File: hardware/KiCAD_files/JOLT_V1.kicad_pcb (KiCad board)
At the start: 2 copper layers, 71.8 x 48.5 mm, 73 parts, among them J1 Conn_01x04_Pin, J13 Conn_01x05_Pin, J2 Conn_01x10_Socket, J3 Conn_01x04_Pin, J4 XT60-M, J5 Conn_01x13_Socket, SW1 SW_Push, SW2 SW_SPDT, U1 STM32F405RGT6, U2 AMS1117-3.3, U3 PCA9685BS, U4 AMS1117-5.0, U5 ICM-42688-P, Y1 16MHz

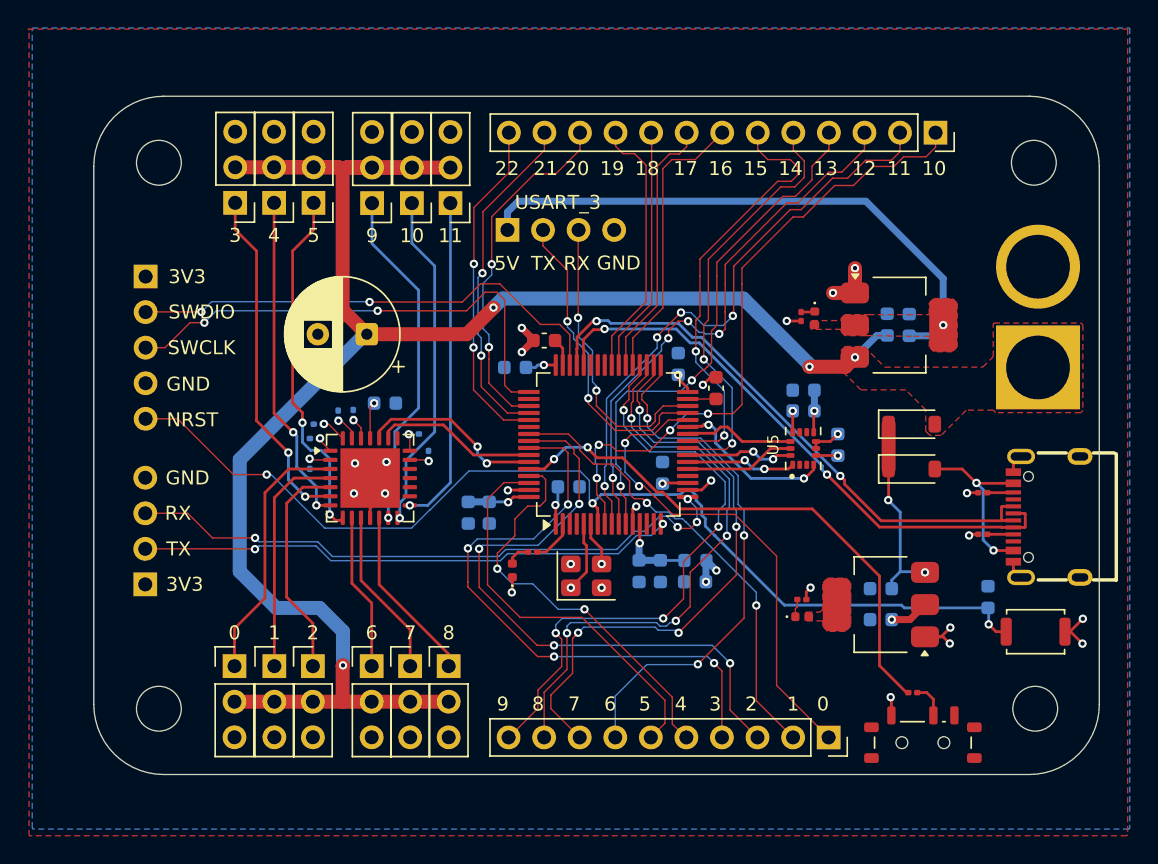
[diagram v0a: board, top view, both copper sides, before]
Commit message: Add new files after review and update readme
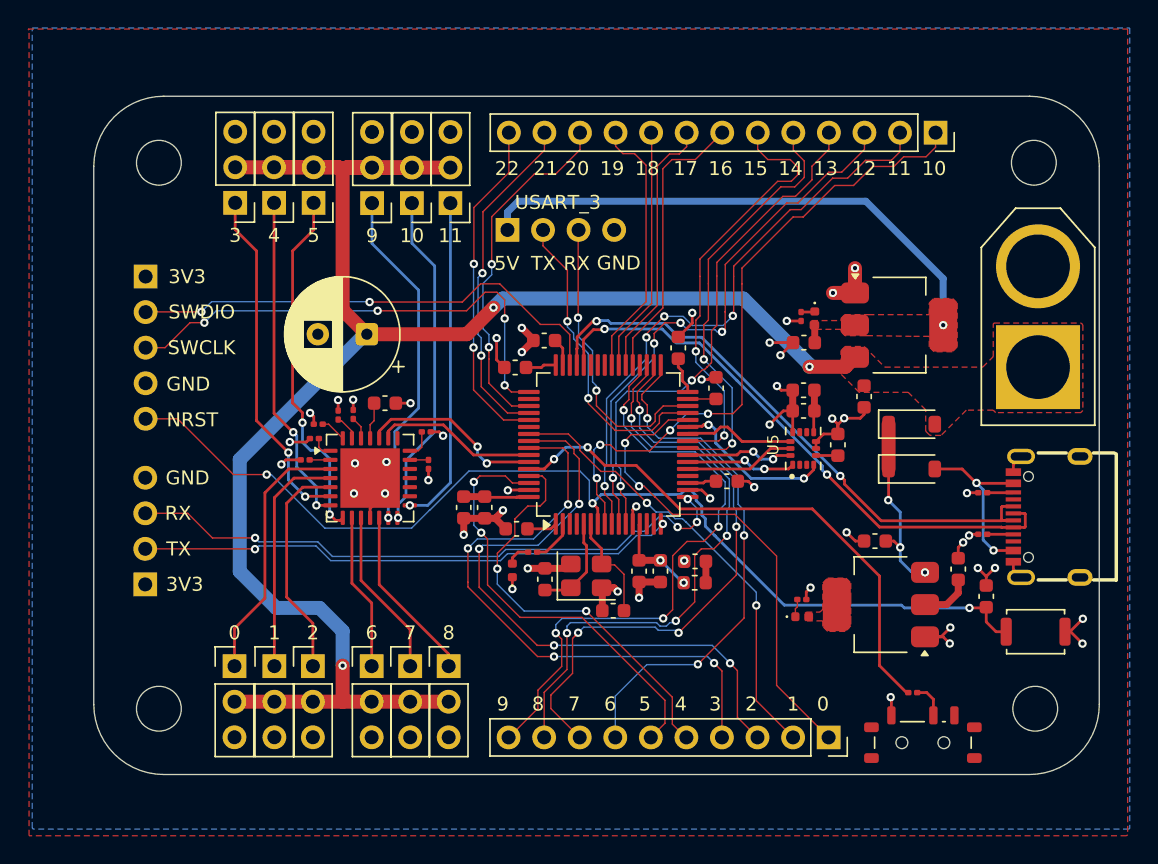
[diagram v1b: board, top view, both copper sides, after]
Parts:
- C1, C10, C11, C12, C13, C15, C16, C19, C2, C20, C21, C22, C23, C3, C4, C5, C6, C7, C8, C9, FB1, J4, R12, R13, R14, R15, R16, R17, R18: moved to F.Cu
- moved C23 7.63 mm to (168.1, 86.8), turned to 180 degrees
- moved C13 6.60 mm to (179.1, 103.0), turned to 90 degrees
- moved C22 5.40 mm to (172.4, 90.7), turned to -90 degrees
- moved C1 4.78 mm to (147.6, 100.2), turned to 180 degrees
- moved C3 4.64 mm to (162.6, 96.8), turned to 0 degrees
- moved C12 3.43 mm to (173.2, 101.0)
- moved C16 2.59 mm to (154.4, 106.0), turned to 180 degrees
- moved C15 1.72 mm to (149.6, 103.8)
- moved FB1 1.59 mm to (160.3, 104.0)
- moved C9 1.46 mm to (160.3, 102.5)
- moved C5 1.15 mm to (159.1, 87.2)
- moved R18 0.86 mm to (141.1, 93.2)
- moved R12 0.64 mm to (141.3, 95.5), turned to -90 degrees
- moved C2 0.50 mm to (145.3, 98.6)
- moved C6 0.50 mm to (143.8, 98.6)
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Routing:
- net GND: track 34.3 -> 79.3 mm, vias 26 -> 49
- net /Main/HSE_OUT: track 3.29 -> 7.69 mm, vias 1 -> 0
- net SERVO_PWR: track 131.7 -> 127.7 mm, vias 4 -> 3
- net /Main/GPIO5: track 28.7 -> 31.2 mm, vias 0 -> 2
- net /Main/HSE_IN: track 5.29 -> 7.03 mm, vias 1 -> 0
- net +5V: track 41.1 -> 39.7 mm
- net Net-(U3-A5): track 1.22 -> 2.06 mm, vias 1 -> 0
- net Net-(D4-K): track 14.2 -> 13.4 mm, vias 2 -> 3
- net /Main/GPIO9: track 43.2 -> 43.9 mm
- net /Main/GPIO4: track 29.2 -> 29.9 mm
- net +3.3VA: track 5.86 -> 6.47 mm, vias 1 -> 2
- net /Main/GPIO1: track 33.1 -> 32.6 mm
- net /Main/GPIO8: track 41.9 -> 42.4 mm
- net Net-(U3-A3): track 1.20 -> 1.55 mm, vias 1 -> 0
- net +3.3V: track 25.4 -> 25.6 mm, vias 11 -> 0
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
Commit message: Update files
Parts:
- H1, H2, H3, H4: footprint MountingHole:MountingHole_3.2mm_M3 -> MountingHole:MountingHole_3.2mm_M3_Pad_Via

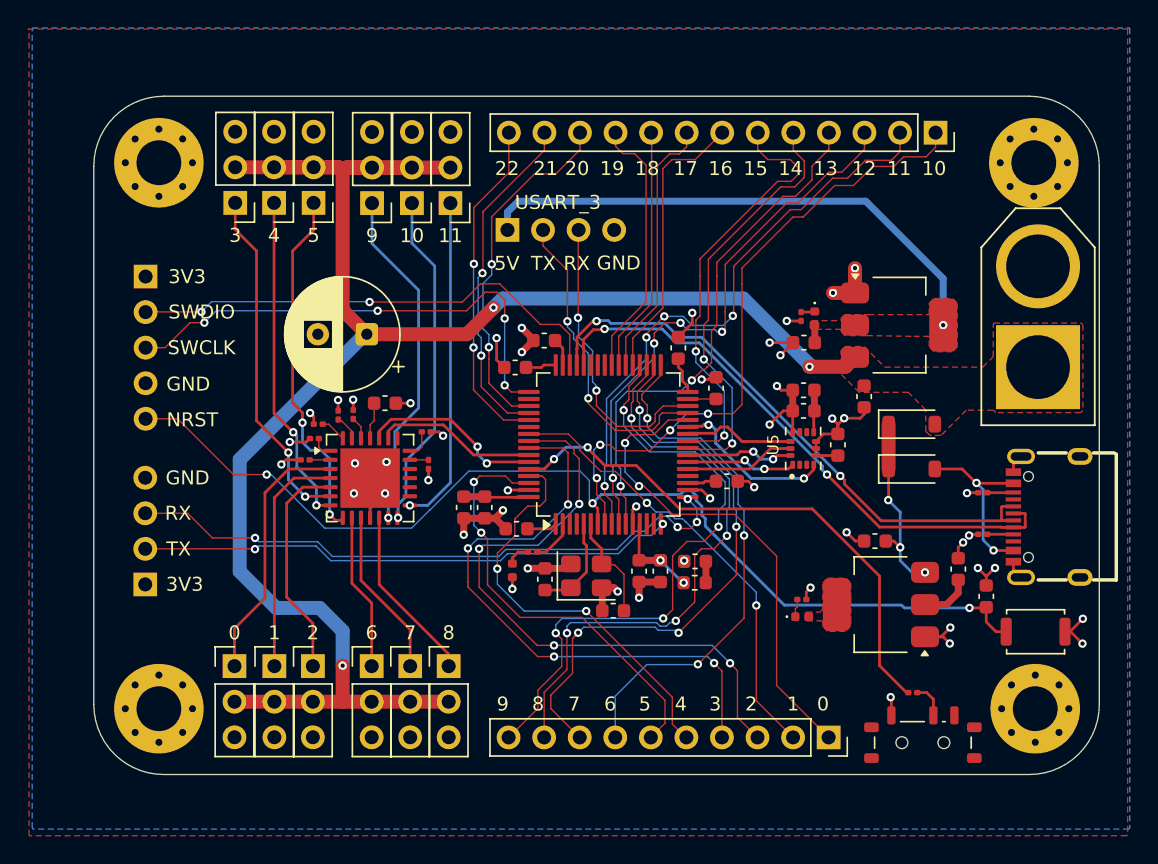
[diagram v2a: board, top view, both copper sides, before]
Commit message: Add 4 layer pcb and update readme
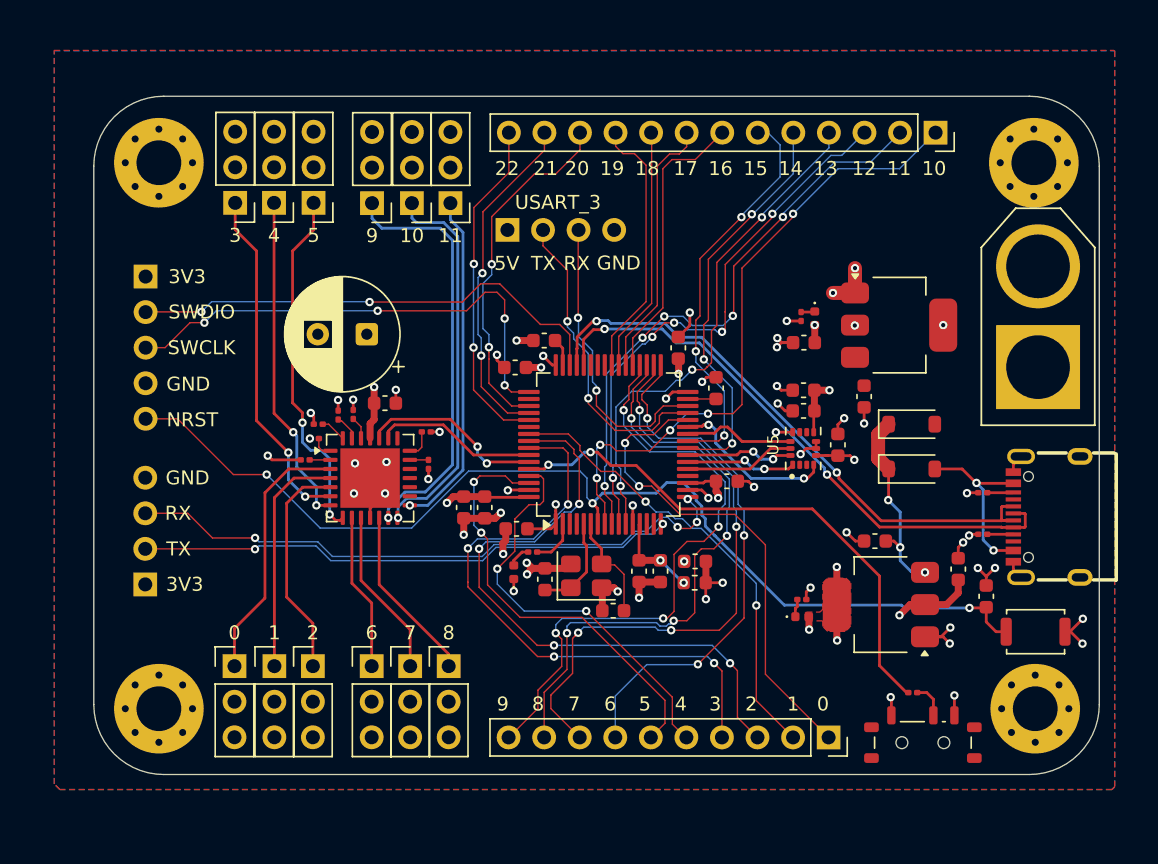
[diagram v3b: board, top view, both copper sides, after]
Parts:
- moved D1 0.16 mm to (147.3, 103.2)
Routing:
- net SERVO_PWR: track 127.7 -> 0.00 mm, vias 3 -> 0
- net +5V: track 39.7 -> 1.33 mm, vias 1 -> 3
- net +3.3V: track 25.6 -> 45.6 mm, vias 0 -> 17
- net GND: track 79.3 -> 71.5 mm, vias 49 -> 52
- net /Servo_Controller/SERVO_9: track 24.8 -> 30.1 mm
- net /Servo_Controller/SERVO_10: track 24.2 -> 27.6 mm
- net /Main/GPIO15: track 30.9 -> 28.8 mm, vias 2 -> 3
- net /Main/GPIO7: track 42.8 -> 44.2 mm
- net /Main/GPIO14: track 30.3 -> 29.2 mm, vias 2 -> 3
- net /Servo_Controller/SERVO_11: track 23.5 -> 24.3 mm
- net /Main/GPIO13: track 37.4 -> 36.7 mm, vias 2 -> 3
- net /Main/GPIO10: track 46.1 -> 45.4 mm, vias 4 -> 5
- net /Main/GPIO11: track 42.5 -> 41.8 mm, vias 4 -> 5
- net Net-(D4-K): track 13.4 -> 14.1 mm
- net /Main/GPIO12: track 40.0 -> 39.6 mm, vias 4 -> 5
- added copper zone on In1.Cu, net +3.3V
- added copper zone on B.Cu, net +5V
- added copper zone on In2.Cu, net GND
- removed copper zone on F.Cu, net +5V
- removed copper zone on B.Cu, net GND
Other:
- copper layers 2 -> 4

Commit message: Add updated kicad files
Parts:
- moved R12 0.35 mm to (141.1, 95.2)
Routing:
- net SERVO_PWR: track 0.00 -> 138.4 mm, vias 0 -> 5
- net +5V: track 1.33 -> 40.4 mm, vias 3 -> 2
- net GND: track 71.5 -> 95.7 mm
- net +3.3V: track 45.6 -> 61.5 mm, vias 17 -> 10
- net /Main/GPIO6: track 37.9 -> 38.7 mm, vias 3 -> 4
- net /Main/GPIO20: track 25.4 -> 24.7 mm
- net Net-(D4-K): track 14.1 -> 13.4 mm, vias 3 -> 4
- net /Main/USART2_TX: track 38.6 -> 38.8 mm, vias 2 -> 4
- net I2C_SCL: track 11.6 -> 11.7 mm, vias 0 -> 2
- net Net-(U1-BOOT0): vias 2 -> 4
- net /Main/USART2_RX: vias 4 -> 6
- net /Main/GPIO0: vias 2 -> 4
- added copper zone on B.Cu, net GND
- removed copper zone on In1.Cu, net +3.3V
- removed copper zone on B.Cu, net +5V
- removed copper zone on In2.Cu, net GND
- removed copper zone on F.Cu, net SERVO_PWR
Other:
- copper layers 4 -> 2
